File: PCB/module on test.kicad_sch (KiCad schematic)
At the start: 71 parts, among them J2 Conn_01x08, J3 Conn_01x08, U1 THS4281, U2 STM32F405RGT6, U3 THS4281, U5 THS4281, U6 THS4281

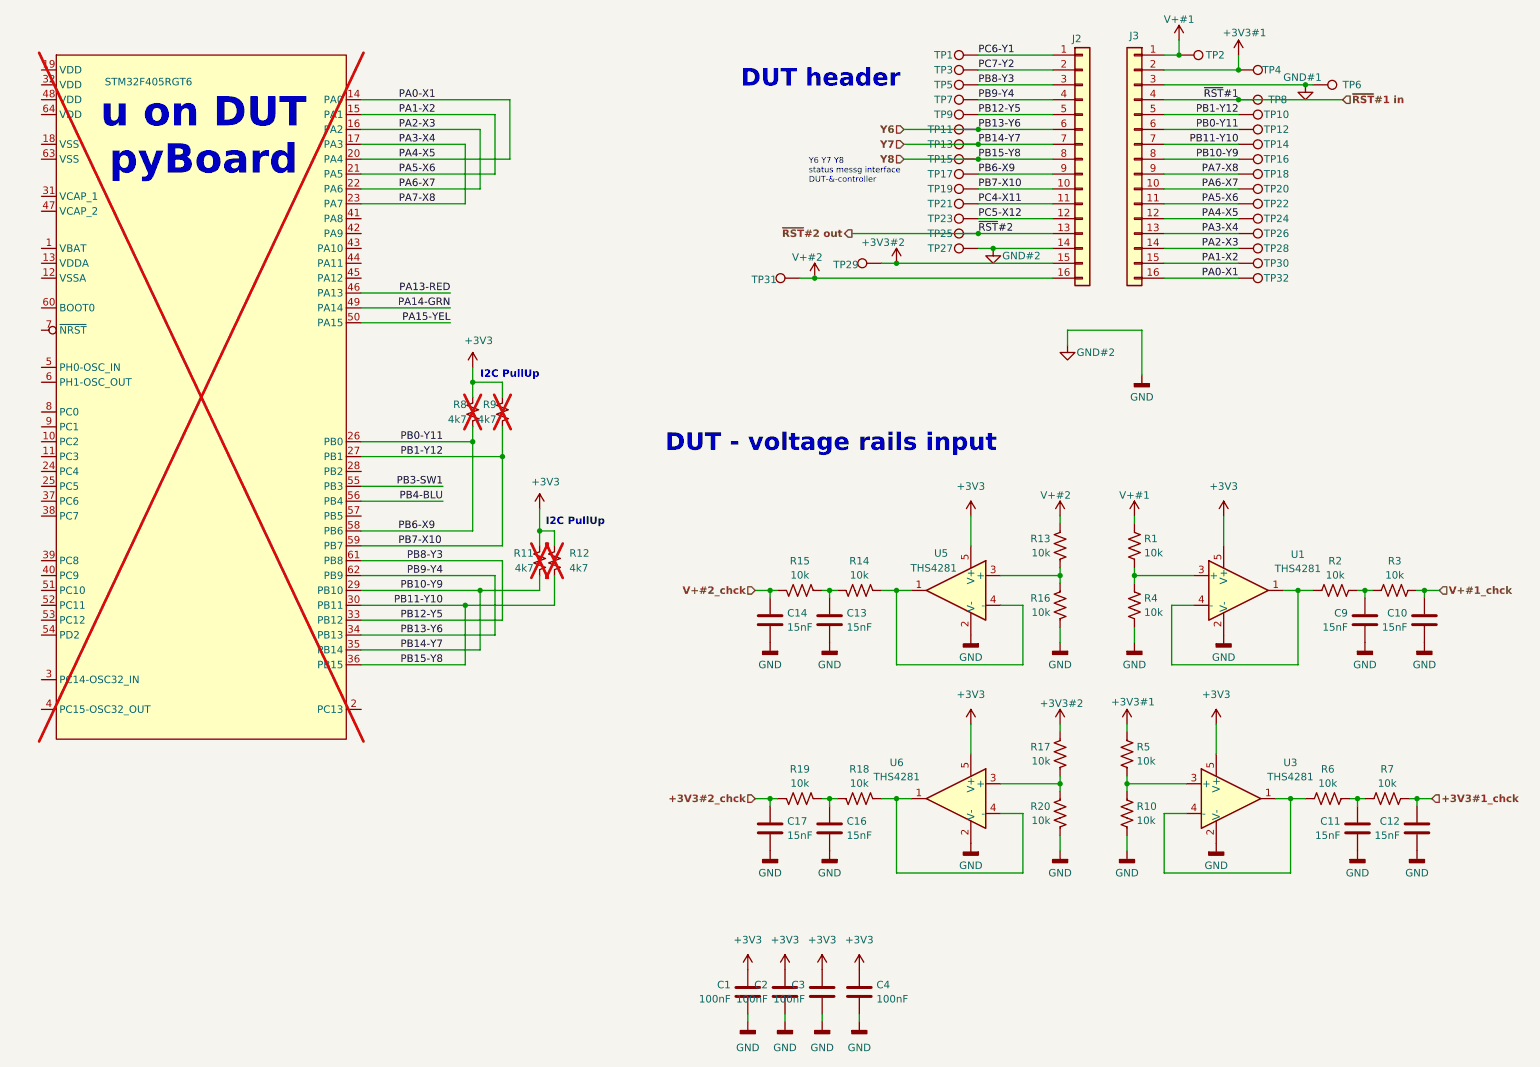
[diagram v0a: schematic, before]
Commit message: após revisão do Filipe
- adicionados LEDs PASS & FAIL para sinalizar fim teste
- modificadasa Designators de LEDs para estar coerente na BOM
- unidos pares de IOs do pyBoard q faltavam
- reimensionado divisor resistivo para ADC-In
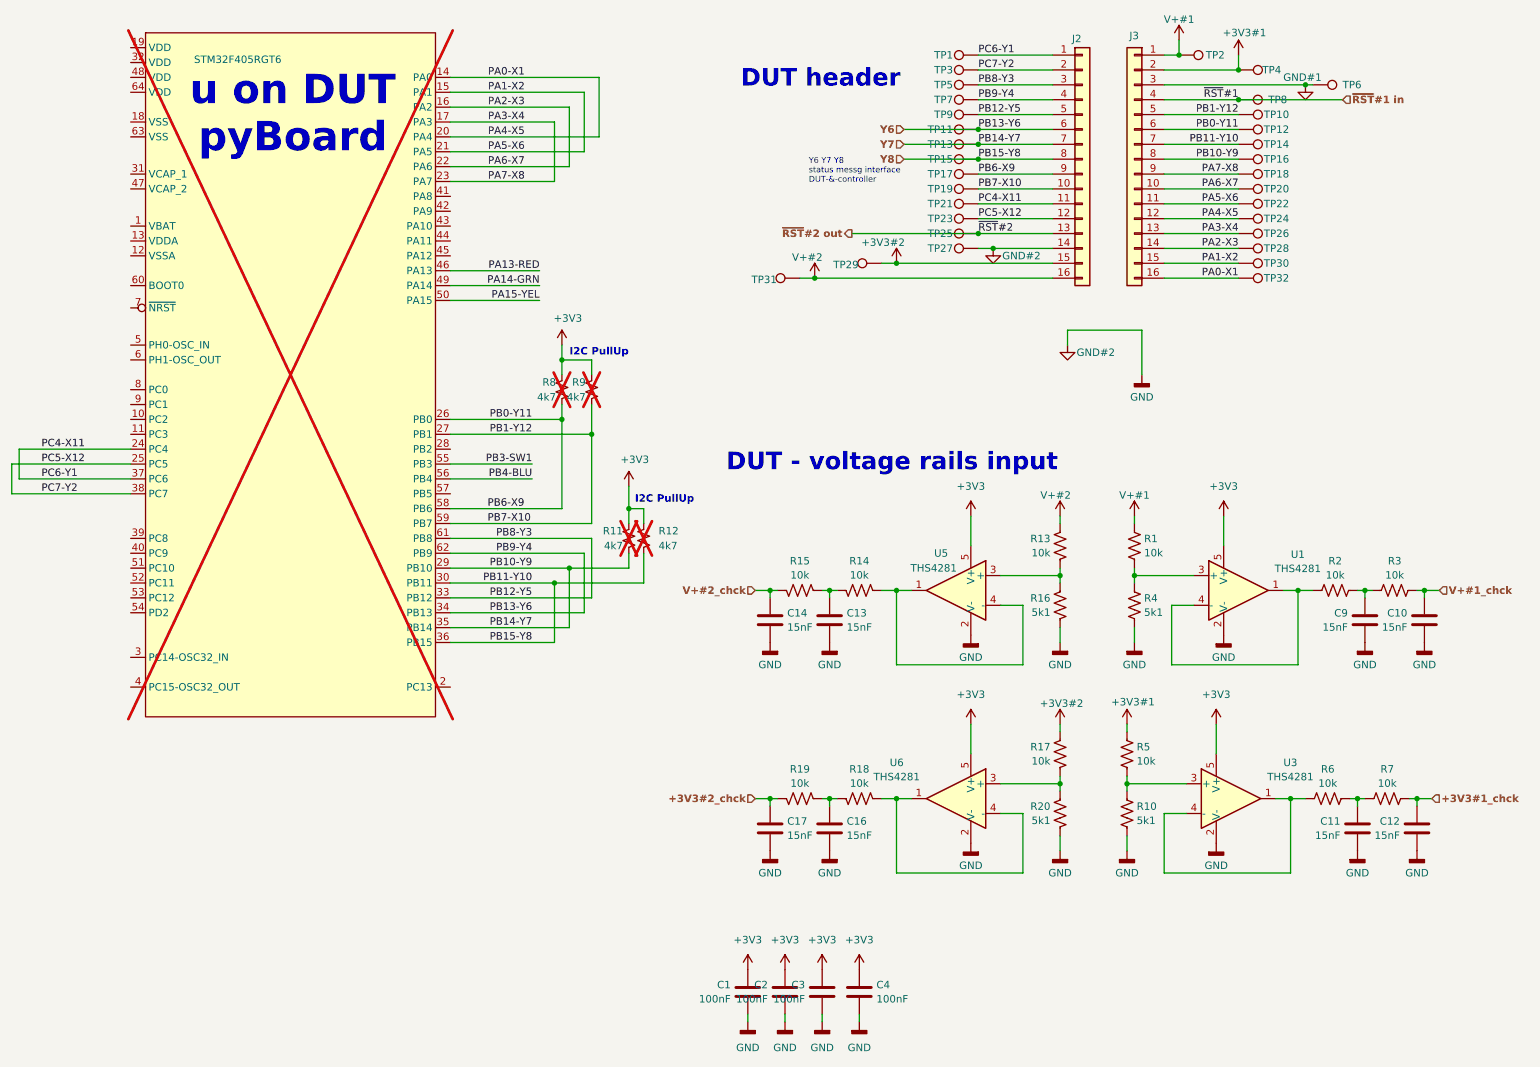
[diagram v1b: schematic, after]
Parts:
- C1, C2, C3, C4: footprint Capacitor_SMD:C_0402_1005Metric_Pad0.74x0.62mm_HandSolder -> Capacitor_SMD:C_0402_1005Metric; MPN C1005X7R1E104K050BB -> CGA2B3X7R1H104K050BB; OEPSPN OEPS010050 -> OEPS010016
- R1, R13, R14, R15, R17, R18, R19, R2, R3, R5, R6, R7: MPN CRCW040210K0FKED -> CPF0402B10KE1; OEPSPN OEPS020030 -> OEPS020043
- R10, R16, R20, R4: value 10k -> 5k1; MPN CRCW040210K0FKED -> ERJ-2RKF5101X; OEPSPN OEPS020030 -> OEPS020173
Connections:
- net PC6-Y1 is gone; now on net PC4-X11: J2.1 (Pin_1), TP1.1
- net PC7-Y2 is gone; now on net PC5-X12: J2.2 (Pin_2), TP3.1
- net PC4-X11: now also U2.24 (PC4), U2.37 (PC6)
- net PC5-X12: now also U2.25 (PC5), U2.38 (PC7)
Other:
- moved on the sheet: R11, R12, R8, R9

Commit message: modificado nome projecto - OE PyBoard tester
OE PyBoard tester
- feita nova anotação para componentes ficarem com Referências sem jumps
- novo nome às Symbol & Footprint Libraries
- optimizadas link de componentes & footprints às novas Libraries
- retirado campo 'values' de Fab. Layer
- gerados novos ficheiros de produção: Gerbers & Drills & P&P & .d356 & BOM
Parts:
- C15: renamed from C14; ASSEMBLY Yes -> (none)
- C16: renamed from C13; ASSEMBLY Yes -> (none)
- C17: renamed from C9; ASSEMBLY Yes -> (none)
- C18: renamed from C10; ASSEMBLY Yes -> (none)
- C19: renamed from C17; ASSEMBLY Yes -> (none)
- C20: renamed from C16; ASSEMBLY Yes -> (none)
- C21: renamed from C11; ASSEMBLY Yes -> (none)
- C22: renamed from C12; ASSEMBLY Yes -> (none)
- C23: renamed from C1; ASSEMBLY Yes -> (none)
- C24: renamed from C2; ASSEMBLY Yes -> (none)
- C25: renamed from C3; ASSEMBLY Yes -> (none)
- C26: renamed from C4; ASSEMBLY Yes -> (none)
- R22: renamed from R13; ASSEMBLY Yes -> (none)
- R23: renamed from R1; ASSEMBLY Yes -> (none)
- R24: renamed from R15; ASSEMBLY Yes -> (none)
- R25: renamed from R14; ASSEMBLY Yes -> (none)
- R26: renamed from R2; ASSEMBLY Yes -> (none)
- R27: renamed from R3; ASSEMBLY Yes -> (none)
- R28: renamed from R16; ASSEMBLY Yes -> (none)
- R29: renamed from R4; ASSEMBLY Yes -> (none)
- R30: renamed from R17; ASSEMBLY Yes -> (none)
- R31: renamed from R5; ASSEMBLY Yes -> (none)
- R32: renamed from R19; ASSEMBLY Yes -> (none)
- R33: renamed from R18; ASSEMBLY Yes -> (none)
- R34: renamed from R6; ASSEMBLY Yes -> (none)
- R35: renamed from R7; ASSEMBLY Yes -> (none)
- R36: renamed from R20; ASSEMBLY Yes -> (none)
- R37: renamed from R10; ASSEMBLY Yes -> (none)
- TP1, TP10, TP11, TP12, TP13, TP14, TP15, TP16, TP17, TP18, TP19, TP2, TP20, TP21, TP22, TP23, TP24, TP25, TP26, TP27, TP28, TP29, TP3, TP30, TP31, TP32, TP4, TP5, TP6, TP7, TP8, TP9: OEPSPN (none) -> OEPS000000
- U4: renamed from U2; symbol MicroPython SymbLib:STM32F405RGT6 -> PyBoardTester:STM32F405RGT6
- U5: symbol _symbolLib:THS4281DBVT -> PyBoardTester:THS4281DBVT
- U6: renamed from U1; symbol _symbolLib:THS4281DBVT -> PyBoardTester:THS4281DBVT
- U7: renamed from U6; symbol _symbolLib:THS4281DBVT -> PyBoardTester:THS4281DBVT
- U8: renamed from U3; symbol _symbolLib:THS4281DBVT -> PyBoardTester:THS4281DBVT
- renumbered J2 to J4, J3 to J5, R8 to R18, R9 to R19, R11 to R20, R12 to R21
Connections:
- no-connect marks 0 -> 5

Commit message: synchronizing with main branch
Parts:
- R22, R23, R24, R25, R26, R27, R30, R31, R32, R33, R34, R35: value 10k -> 10k 0.1%
- R28, R29, R36, R37: value 5k1 -> 5k1 0.1%; MPN ERJ-2RKF5101X -> RT0402BRD075K1L; OEPSPN OEPS020173 -> OEPS020203
- TP12: now not fitted
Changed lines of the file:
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@@
 		(in_bom no)
 		(on_board yes)
-		(dnp no)
+		(dnp yes)
 		(property "Reference" "TP12"
 			(at 230.378 33.02 90)
@@
 			)
 		)
-		(property "Value" "10k"
+		(property "Value" "10k 0.1%"
 			(at 151.13 109.1508 90)
 			(effects
@@
 			)
 		)
-		(property "Value" "10k"
+		(property "Value" "10k 0.1%"
 			(at 193.929 105.3521 0)
 			(effects
@@
 			)
 		)
-		(property "Value" "10k"
+		(property "Value" "10k 0.1%"
 			(at 161.29 109.1508 90)
 			(effects
@@
 		(on_board yes)
 		(dnp no)
-		(fields_autoplaced yes)
 		(property "Reference" "R36"
 			(at 193.929 148.6478 0)
@@
 			)
 		)
-		(property "Value" "5k1"
-			(at 193.929 151.0721 0)
+		(property "Value" "5k1 0.1%"
+			(at 198.882 153.924 90)
 			(effects
 				(font
@@
 			)
 		)
-		(property "Description" "SMD 0402 5.1kΩ ±1% 0.100W"
+		(property "Description" "SMD 0402 5.1kΩ ±0.1% 0.063W"
 			(at 195.58 149.86 0)
 			(effects
@@
 			)
 		)
-		(property "MPN" "ERJ-2RKF5101X"
+		(property "MPN" "RT0402BRD075K1L"
 			(at 186.817 152.908 0)
 			(effects
@@
 			)
 		)
-		(property "OEPSPN" "OEPS020173"
+		(property "OEPSPN" "OEPS020203"
 			(at 195.58 149.86 0)
 			(effects
@@
 			)
 		)
-		(property "Value" "10k"
+		(property "Value" "10k 0.1%"
 			(at 241.3 144.7108 90)
 			(effects
@@
 		(on_board yes)
 		(dnp no)
-		(fields_autoplaced yes)
 		(property "Reference" "R29"
 			(at 209.931 113.0878 0)
@@
 			)
 		)
-		(property "Value" "5k1"
-			(at 209.931 115.5121 0)
+		(property "Value" "5k1 0.1%"
+			(at 205.74 118.364 90)
 			(effects
 				(font
@@
 			)
 		)
-		(property "Description" "SMD 0402 5.1kΩ ±1% 0.100W"
+		(property "Description" "SMD 0402 5.1kΩ ±0.1% 0.063W"
 			(at 208.28 114.3 0)
 			(effects
@@
 			)
 		)
-		(property "MPN" "ERJ-2RKF5101X"
+		(property "MPN" "RT0402BRD075K1L"
 			(at 217.043 117.348 0)
 			(effects
@@
 			)
 		)
-		(property "OEPSPN" "OEPS020173"
+		(property "OEPSPN" "OEPS020203"
 			(at 208.28 114.3 0)
 			(effects
@@
 			)
 		)
-		(property "Value" "10k"
+		(property "Value" "10k 0.1%"
 			(at 151.13 144.7108 90)
 			(effects
@@
 			)
 		)
-		(property "Value" "10k"
+		(property "Value" "10k 0.1%"
 			(at 251.46 144.7108 90)
 			(effects
@@
 			)
 		)
-		(property "Value" "10k"
+		(property "Value" "10k 0.1%"
 			(at 209.931 105.3521 0)
 			(effects
@@
 			)
 		)
-		(property "Value" "10k"
+		(property "Value" "10k 0.1%"
 			(at 252.73 109.1508 90)
 			(effects
@@
 			)
 		)
-		(property "Value" "10k"
+		(property "Value" "10k 0.1%"
 			(at 208.661 140.9121 0)
 			(effects
@@
 			)
 		)
-		(property "Value" "10k"
+		(property "Value" "10k 0.1%"
 			(at 242.57 109.1508 90)
 			(effects
@@
 		(on_board yes)
 		(dnp no)
-		(fields_autoplaced yes)
 		(property "Reference" "R30"
 			(at 193.929 138.4878 0)
@@
 			)
 		)
-		(property "Value" "10k"
+		(property "Value" "10k 0.1%"
 			(at 193.929 140.9121 0)
 			(effects
@@
 		(on_board yes)
 		(dnp no)
-		(fields_autoplaced yes)
 		(property "Reference" "R28"
 			(at 193.929 113.0878 0)
@@
 			)
 		)
-		(property "Value" "5k1"
-			(at 193.929 115.5121 0)
+		(property "Value" "5k1 0.1%"
+			(at 198.628 118.618 90)
 			(effects
 				(font
@@
 			)
 		)
-		(property "Description" "SMD 0402 5.1kΩ ±1% 0.100W"
+		(property "Description" "SMD 0402 5.1kΩ ±0.1% 0.063W"
 			(at 195.58 114.3 0)
 			(effects
@@
 			)
 		)
-		(property "MPN" "ERJ-2RKF5101X"
+		(property "MPN" "RT0402BRD075K1L"
 			(at 186.817 117.348 0)
 			(effects
@@
 			)
 		)
-		(property "OEPSPN" "OEPS020173"
+		(property "OEPSPN" "OEPS020203"
 			(at 195.58 114.3 0)
 			(effects
@@
 			)
 		)
-		(property "Value" "10k"
+		(property "Value" "10k 0.1%"
 			(at 161.29 144.7108 90)
 			(effects
@@
 		(on_board yes)
 		(dnp no)
-		(fields_autoplaced yes)
 		(property "Reference" "R37"
 			(at 208.661 148.6478 0)
@@
 			)
 		)
-		(property "Value" "5k1"
-			(at 208.661 151.0721 0)
+		(property "Value" "5k1 0.1%"
+			(at 203.708 153.67 90)
 			(effects
 				(font
@@
 			)
 		)
-		(property "Description" "SMD 0402 5.1kΩ ±1% 0.100W"
+		(property "Description" "SMD 0402 5.1kΩ ±0.1% 0.063W"
 			(at 207.01 149.86 0)
 			(effects
@@
 			)
 		)
-		(property "MPN" "ERJ-2RKF5101X"
+		(property "MPN" "RT0402BRD075K1L"
 			(at 215.773 152.908 0)
 			(effects
@@
 			)
 		)
-		(property "OEPSPN" "OEPS020173"
+		(property "OEPSPN" "OEPS020203"
 			(at 207.01 149.86 0)
 			(effects
